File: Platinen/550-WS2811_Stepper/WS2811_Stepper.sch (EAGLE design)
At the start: 50 parts, among them CON1 End SW1, CON2 End SW2, CON3 End SW1H, CON4 STEPPER_CON, CON5 End SW2H, CON6 NEMA17, CON7 LED, IC1 4017N, J10 , M1 BOARD_A4988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

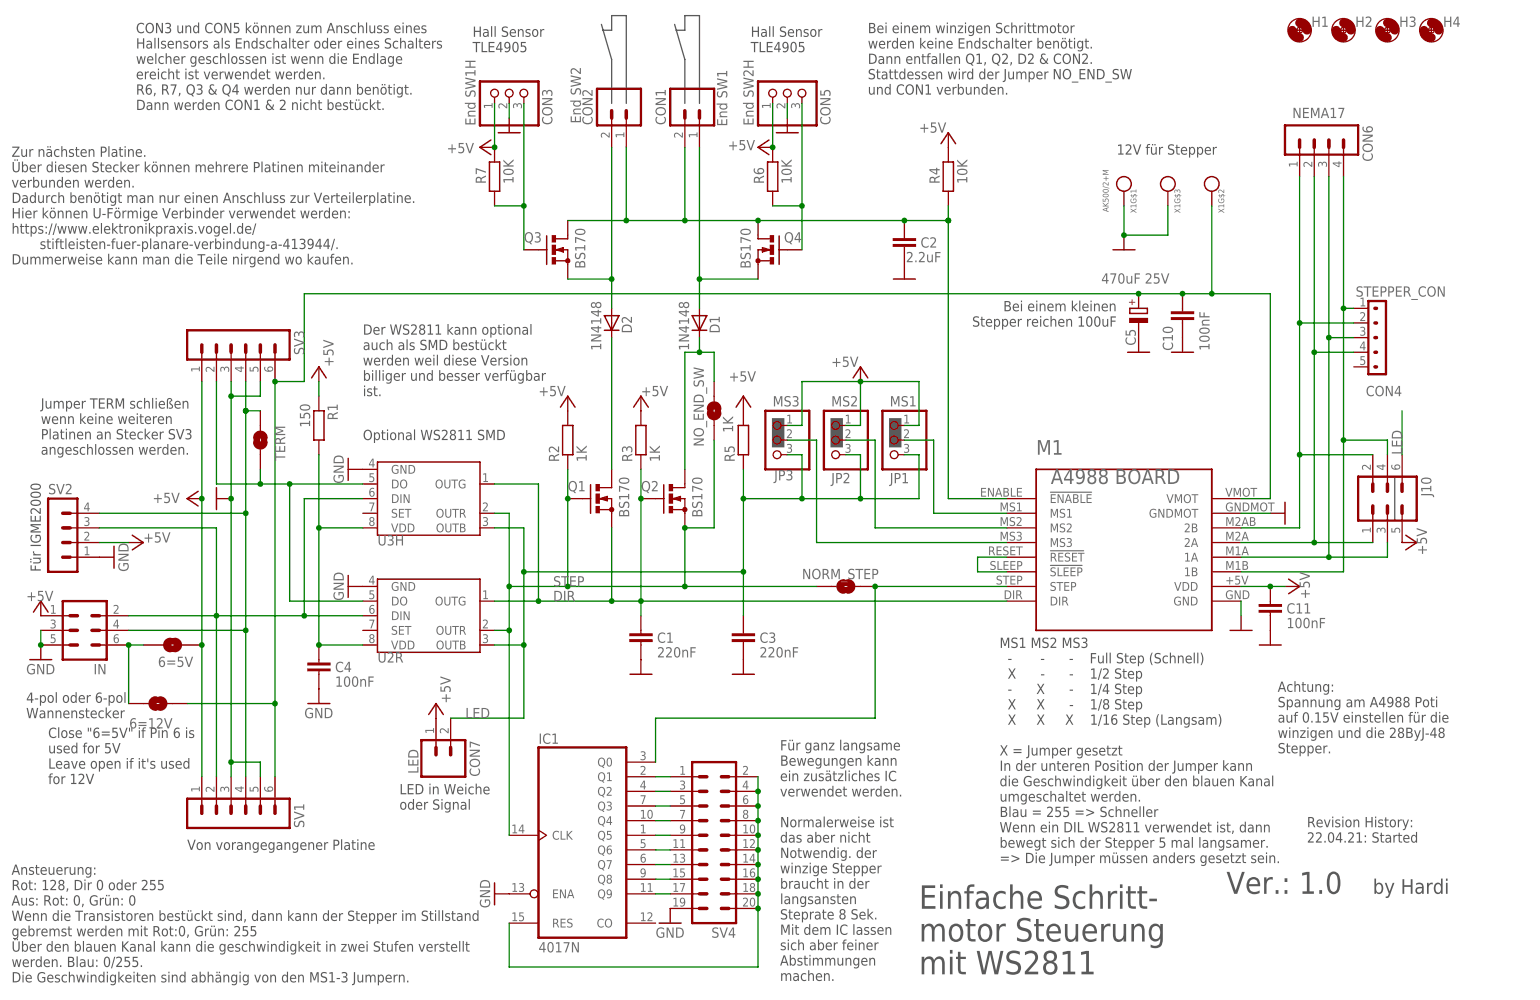
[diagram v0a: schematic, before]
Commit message: Corrected missing 4017 Power Supply
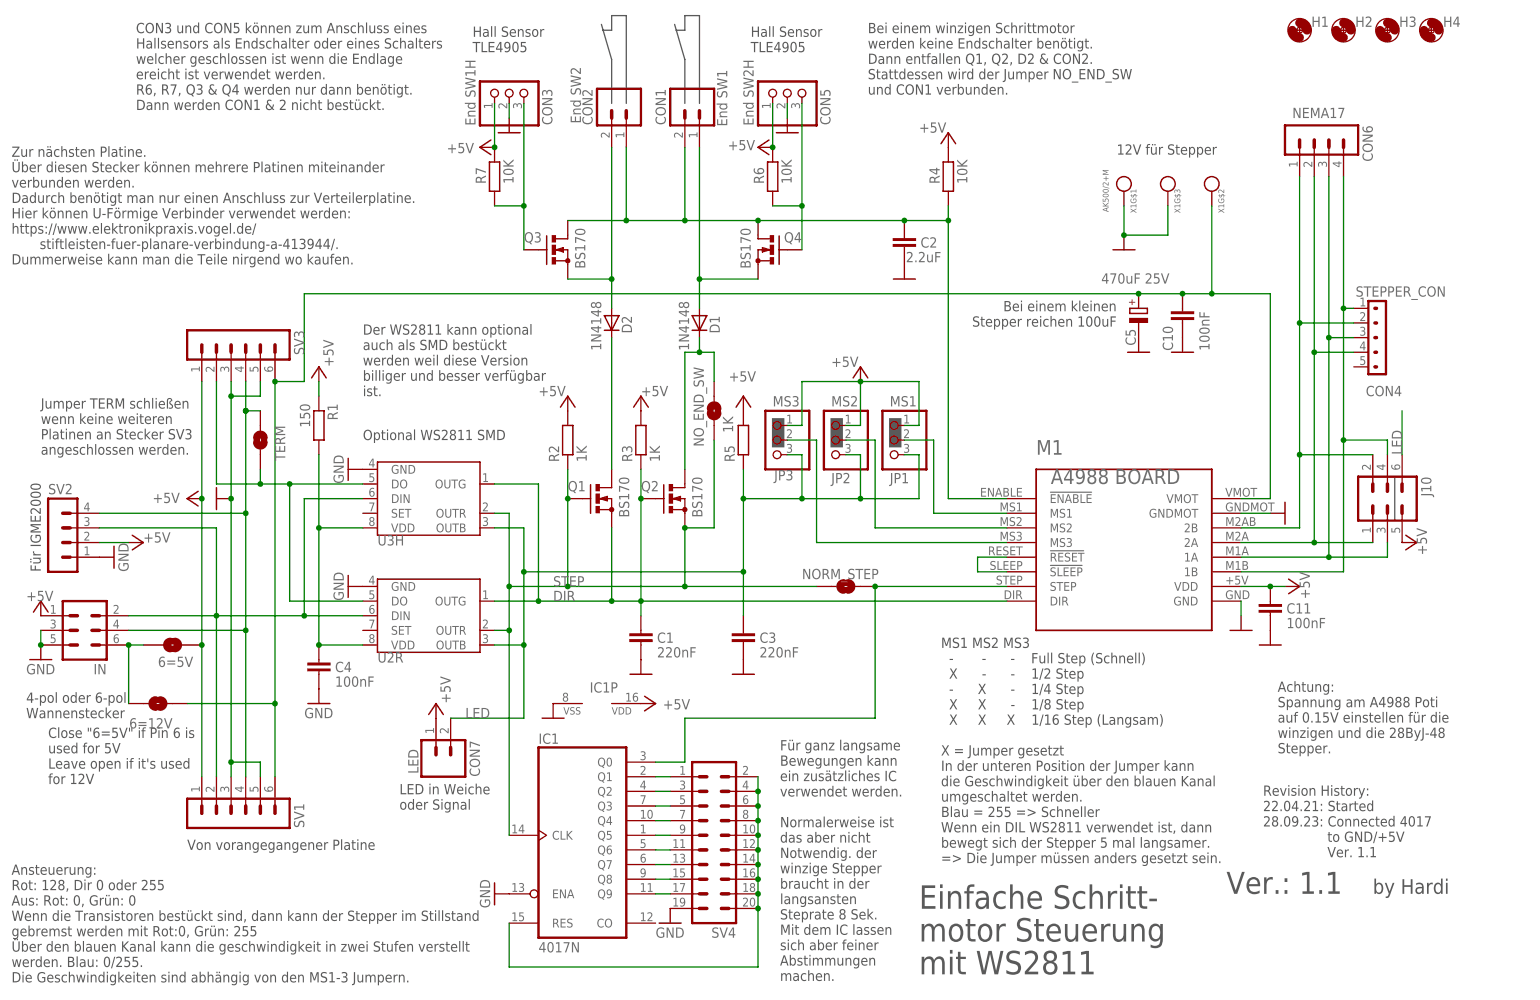
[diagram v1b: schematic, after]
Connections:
- net +5V: now also IC1P.VDD
- net GND: now also IC1P.VSS
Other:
- note added: "Revision History: 22.04.21: Started 28.09.23: Connected 4017 to GND/+5V Ver. 1.1"
- note added: "Ver.: 1.1"
- note removed: "Revision History: 22.04.21: Started"
- note removed: "Ver.: 1.0"
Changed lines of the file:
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@@
 <drawing>
 <settings>
-<setting alwaysvectorfont="yes"/>
+<setting alwaysvectorfont="no"/>
 <setting verticaltext="up"/>
 </settings>
@@
 <part name="J10" library="con-harting-ml" deviceset="ML6" device="" value=" "/>
 <part name="P+14" library="supply1" library_urn="urn:adsk.eagle:library:371" deviceset="+5V" device=""/>
+<part name="GND17" library="supply1" deviceset="GND" device=""/>
+<part name="P+15" library="supply1" library_urn="urn:adsk.eagle:library:371" deviceset="+5V" device=""/>
 </parts>
 <sheets>
@@
 Platinen an Stecker SV3
 angeschlossen werden.</text>
-<text x="229.87" y="29.21" size="1.778" layer="97">Revision History:
-22.04.21: Started</text>
+<text x="222.25" y="26.67" size="1.778" layer="97">Revision History:
+22.04.21: Started
+28.09.23: Connected 4017
+                to GND/+5V
+                Ver. 1.1</text>
 <wire x1="109.22" y1="157.48" x2="109.22" y2="165.1" width="0.1524" layer="97"/>
 <wire x1="109.22" y1="165.1" x2="107.442" y2="171.196" width="0.1524" layer="97"/>
@@
 <wire x1="121.92" y1="172.72" x2="124.46" y2="172.72" width="0.1524" layer="97"/>
 <wire x1="124.46" y1="172.72" x2="124.46" y2="157.48" width="0.1524" layer="97"/>
-<text x="176.53" y="64.77" size="1.778" layer="97" align="top-left">MS1 MS2 MS3
+<text x="166.37" y="64.77" size="1.778" layer="97" align="top-left">MS1 MS2 MS3
   -       -      -    Full Step (Schnell)
   X      -      -    1/2 Step
@@
 <text x="196.85" y="148.59" size="1.778" layer="97">12V für Stepper</text>
 <text x="241.3" y="20.32" size="2.54" layer="92">by Hardi</text>
-<text x="215.9" y="20.32" size="3.81" layer="97">Ver.: 1.0</text>
+<text x="215.9" y="20.32" size="3.81" layer="97">Ver.: 1.1</text>
 <text x="162.56" y="6.35" size="4.064" layer="97" distance="40">Einfache Schritt-
 motor Steuerung
@@
 <attribute name="VALUE" x="248.92" y="83.82" size="1.778" layer="96" rot="R270"/>
 </instance>
+<instance part="IC1" gate="P" x="106.68" y="53.34" smashed="yes" rot="R270">
+<attribute name="NAME" x="105.41" y="55.245" size="1.778" layer="95"/>
+</instance>
+<instance part="GND17" gate="1" x="99.06" y="50.8" smashed="yes" rot="MR0"/>
+<instance part="P+15" gate="1" x="116.84" y="53.34" smashed="yes" rot="R270">
+<attribute name="VALUE" x="118.11" y="52.324" size="1.778" layer="96"/>
+</instance>
 </instances>
 <busses>
@@
 <pinref part="GND16" gate="1" pin="GND"/>
 </segment>
+<segment>
+<pinref part="IC1" gate="P" pin="VSS"/>
+<pinref part="GND17" gate="1" pin="GND"/>
+</segment>
 </net>
 <net name="+5V" class="0">
@@
 <pinref part="J10" gate="1" pin="5"/>
 <pinref part="P+14" gate="1" pin="+5V"/>
+</segment>
+<segment>
+<pinref part="IC1" gate="P" pin="VDD"/>
+<pinref part="P+15" gate="1" pin="+5V"/>
 </segment>
 </net>
@@
 <wire x1="137.16" y1="139.7" x2="142.24" y2="139.7" width="0.1524" layer="91"/>
 <junction x="142.24" y="139.7"/>
-</segment>
-</net>
-<net name="N$17" class="0">
-<segment>
-<junction x="167.64" y="137.16"/>
 </segment>
 </net>
@@
 <segment>
 <pinref part="IC1" gate="A" pin="Q0"/>
-<wire x1="116.84" y1="43.18" x2="116.84" y2="50.8" width="0.1524" layer="91"/>
 <pinref part="M1" gate="G$1" pin="STEP"/>
 <wire x1="177.8" y1="73.66" x2="154.94" y2="73.66" width="0.1524" layer="91"/>
@@
 <pinref part="NORM_STEP" gate="1" pin="2"/>
 <junction x="154.94" y="73.66"/>
-<wire x1="116.84" y1="50.8" x2="154.94" y2="50.8" width="0.1524" layer="91"/>
+<wire x1="121.92" y1="50.8" x2="154.94" y2="50.8" width="0.1524" layer="91"/>
+<wire x1="116.84" y1="43.18" x2="121.92" y2="43.18" width="0.1524" layer="91"/>
+<wire x1="121.92" y1="43.18" x2="121.92" y2="50.8" width="0.1524" layer="91"/>
 </segment>
 </net>
@@
 </sheet>
 </sheets>
+<errors>
+</errors>
 </schematic>
 </drawing>

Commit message: added missing Power-Pins IC1
added missing Power-Pins IC1
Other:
- note added: "Revision History: 12.03.2026: added missing Power-Pins IC1 22.04.2021: Started"
- note added: "Ver.: 1.2"
- note removed: "Revision History: 22.04.21: Started 28.09.23: Connected 4017 to GND/+5V Ver. 1.1"
- note removed: "Ver.: 1.1"
- moved on the sheet: IC1P
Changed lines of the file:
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@@
 <part name="J10" library="con-harting-ml" deviceset="ML6" device="" value=" "/>
 <part name="P+14" library="supply1" library_urn="urn:adsk.eagle:library:371" deviceset="+5V" device=""/>
-<part name="GND17" library="supply1" deviceset="GND" device=""/>
 <part name="P+15" library="supply1" library_urn="urn:adsk.eagle:library:371" deviceset="+5V" device=""/>
+<part name="GND17" library="supply1" library_urn="urn:adsk.eagle:library:371" deviceset="GND" device=""/>
 </parts>
 <sheets>
@@
        stiftleisten-fuer-planare-verbindung-a-413944/.
 Dummerweise kann man die Teile nirgend wo kaufen.</text>
-<text x="35.56" y="27.94" size="1.778" layer="97">Von vorangegangener Platine</text>
+<text x="38.1" y="27.94" size="1.778" layer="97">Von vorangegangener Platine</text>
 <text x="66.04" y="106.68" size="1.778" layer="97">Der WS2811 kann optional
 auch als SMD bestückt
@@
 Platinen an Stecker SV3
 angeschlossen werden.</text>
-<text x="222.25" y="26.67" size="1.778" layer="97">Revision History:
-22.04.21: Started
-28.09.23: Connected 4017
-                to GND/+5V
-                Ver. 1.1</text>
+<text x="224.79" y="31.75" size="1.778" layer="97">Revision History:
+12.03.2026: added missing
+Power-Pins IC1
+22.04.2021: Started</text>
 <wire x1="109.22" y1="157.48" x2="109.22" y2="165.1" width="0.1524" layer="97"/>
 <wire x1="109.22" y1="165.1" x2="107.442" y2="171.196" width="0.1524" layer="97"/>
@@
 <wire x1="121.92" y1="172.72" x2="124.46" y2="172.72" width="0.1524" layer="97"/>
 <wire x1="124.46" y1="172.72" x2="124.46" y2="157.48" width="0.1524" layer="97"/>
-<text x="166.37" y="64.77" size="1.778" layer="97" align="top-left">MS1 MS2 MS3
+<text x="173.99" y="64.77" size="1.778" layer="97" align="top-left">MS1 MS2 MS3
   -       -      -    Full Step (Schnell)
   X      -      -    1/2 Step
@@
 <text x="196.85" y="148.59" size="1.778" layer="97">12V für Stepper</text>
 <text x="241.3" y="20.32" size="2.54" layer="92">by Hardi</text>
-<text x="215.9" y="20.32" size="3.81" layer="97">Ver.: 1.1</text>
+<text x="215.9" y="20.32" size="3.81" layer="97">Ver.: 1.2</text>
 <text x="162.56" y="6.35" size="4.064" layer="97" distance="40">Einfache Schritt-
 motor Steuerung
@@
 <attribute name="VALUE" x="248.92" y="83.82" size="1.778" layer="96" rot="R270"/>
 </instance>
-<instance part="IC1" gate="P" x="106.68" y="53.34" smashed="yes" rot="R270">
-<attribute name="NAME" x="105.41" y="55.245" size="1.778" layer="95"/>
-</instance>
-<instance part="GND17" gate="1" x="99.06" y="50.8" smashed="yes" rot="MR0"/>
-<instance part="P+15" gate="1" x="116.84" y="53.34" smashed="yes" rot="R270">
-<attribute name="VALUE" x="118.11" y="52.324" size="1.778" layer="96"/>
+<instance part="IC1" gate="P" x="167.64" y="45.72" smashed="yes">
+<attribute name="NAME" x="166.37" y="45.085" size="1.778" layer="95"/>
+</instance>
+<instance part="P+15" gate="1" x="167.64" y="58.42" smashed="yes">
+<attribute name="VALUE" x="170.18" y="58.42" size="1.778" layer="96" rot="R90"/>
+</instance>
+<instance part="GND17" gate="1" x="167.64" y="33.02" smashed="yes">
+<attribute name="VALUE" x="165.1" y="30.48" size="1.778" layer="96"/>
 </instance>
 </instances>
@@
 <pinref part="IC1" gate="P" pin="VSS"/>
 <pinref part="GND17" gate="1" pin="GND"/>
+<wire x1="167.64" y1="35.56" x2="167.64" y2="38.1" width="0.1524" layer="91"/>
 </segment>
 </net>
@@
 <pinref part="IC1" gate="P" pin="VDD"/>
 <pinref part="P+15" gate="1" pin="+5V"/>
+<wire x1="167.64" y1="55.88" x2="167.64" y2="53.34" width="0.1524" layer="91"/>
 </segment>
 </net>
@@
 <wire x1="137.16" y1="139.7" x2="142.24" y2="139.7" width="0.1524" layer="91"/>
 <junction x="142.24" y="139.7"/>
+</segment>
+</net>
+<net name="N$17" class="0">
+<segment>
+<junction x="167.64" y="137.16"/>
 </segment>
 </net>
@@
 <segment>
 <pinref part="IC1" gate="A" pin="Q0"/>
+<wire x1="116.84" y1="43.18" x2="116.84" y2="50.8" width="0.1524" layer="91"/>
 <pinref part="M1" gate="G$1" pin="STEP"/>
 <wire x1="177.8" y1="73.66" x2="154.94" y2="73.66" width="0.1524" layer="91"/>
@@
 <pinref part="NORM_STEP" gate="1" pin="2"/>
 <junction x="154.94" y="73.66"/>
-<wire x1="121.92" y1="50.8" x2="154.94" y2="50.8" width="0.1524" layer="91"/>
-<wire x1="116.84" y1="43.18" x2="121.92" y2="43.18" width="0.1524" layer="91"/>
-<wire x1="121.92" y1="43.18" x2="121.92" y2="50.8" width="0.1524" layer="91"/>
+<wire x1="116.84" y1="50.8" x2="154.94" y2="50.8" width="0.1524" layer="91"/>
 </segment>
 </net>
@@
 </sheet>
 </sheets>
-<errors>
-</errors>
 </schematic>
 </drawing>
